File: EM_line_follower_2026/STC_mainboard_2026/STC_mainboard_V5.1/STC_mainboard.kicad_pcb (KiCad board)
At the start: 2 copper layers, 105 x 86.5 mm, 114 parts, among them J1 Conn_01x04, J10 Conn_01x04, J11 WirePad, J12 WirePad, J13 Conn_01x02, J14 WirePad, J15 WirePad, J16 WirePad, J2 WirePad, J20 WirePad, J21 WirePad, J23 WirePad, J24 WirePad, J3 WirePad, J4 Conn_01x04, J5 WirePad, J6 WirePad, J7 WirePad, J8 WirePad, J9 Conn_01x04, SW1 SW_Push, SW3 SW_Push, U1 STC16H40K128_CoreBoard, U10 TPS54360DDA, U3 LSM6DSRTR, U4 LM1117-3.3V, U5 OPA2197xD, U6 OPA2197xD, U7 OPA2197xD

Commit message: update V5.1
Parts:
- removed J1: Conn_01x04, Connector_JST:JST_XH_B4B-XH-A_1x04_P2.50mm_Vertical
- added RST: Conn_02x04_Odd_Even, Connector_PinSocket_2.54mm:PinSocket_2x04_P2.54mm_Vertical, F.Cu at (80.7, 209.9)
- added SW2: SW_Push, em1:SW-TH_L21.0-W15.0-KCD1-103, F.Cu at (59.0, 207.0)
- added SW4: SW_Push, em1:SW-TH_L21.0-W15.0-KCD1-103, F.Cu at (126.0, 133.0)
- C5, C6: moved to B.Cu
- moved J10 43.4 mm to (95.7, 209.6), turned to 180 degrees
- moved J4 7.19 mm to (118.9, 207.9)
- moved J9 7.19 mm to (128.8, 207.9)
- moved 1 6.88 mm to (135.8, 151.5)
- moved 111 6.88 mm to (126.9, 151.3)
- moved 11 6.88 mm to (131.5, 149.2)
- moved J13 6.88 mm to (132.5, 144.5)
- moved C2 4.84 mm to (142.5, 138.2)
- moved D22 4.84 mm to (142.5, 150.5)
- moved J20 4.84 mm to (137.5, 137.7)
- moved J21 4.84 mm to (140.0, 137.8)
- moved R60 4.84 mm to (142.3, 148.5)
- moved U9 4.84 mm to (139.4, 143.0)
- moved C12 3.80 mm to (86.4, 178.6)
- moved R10 3.80 mm to (87.2, 176.3)
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- renumbered RV3 to L1, RV2 to L2, RV4 to L3, RV1 to L4, RV5 to L5, L1 to L7
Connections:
- 111 pad 2: +12V -> /Vin
- J13 pad 2: +12V -> /Vin
- U1 pad 2: +5V -> Net-(U1-VCC)
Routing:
- net +5V: track 363.9 -> 301.1 mm
- net /P6.3: track 60.0 -> 8.11 mm
- net /P6.5: track 48.8 -> 11.2 mm
- net /P0.7: track 0.00 -> 32.4 mm
- net Net-(U1-VCC): track 0.00 -> 21.0 mm
- net /Vin: track 0.00 -> 17.6 mm
- net /P4.2: track 21.7 -> 39.0 mm
- net /P6.4: track 78.7 -> 93.5 mm
- net /P6.6: track 77.6 -> 92.3 mm
- net /P5.3: track 20.6 -> 7.45 mm
- net +12V: track 143.0 -> 154.2 mm, vias 0 -> 2
- net /P6.2: track 82.9 -> 92.3 mm
- net /P5.2: track 13.9 -> 7.40 mm
- net /P0.1: track 14.9 -> 9.01 mm
- net /P1.7: track 12.7 -> 17.8 mm
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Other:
- board size 105 x 86.5 mm -> 105 x 92.5 mm

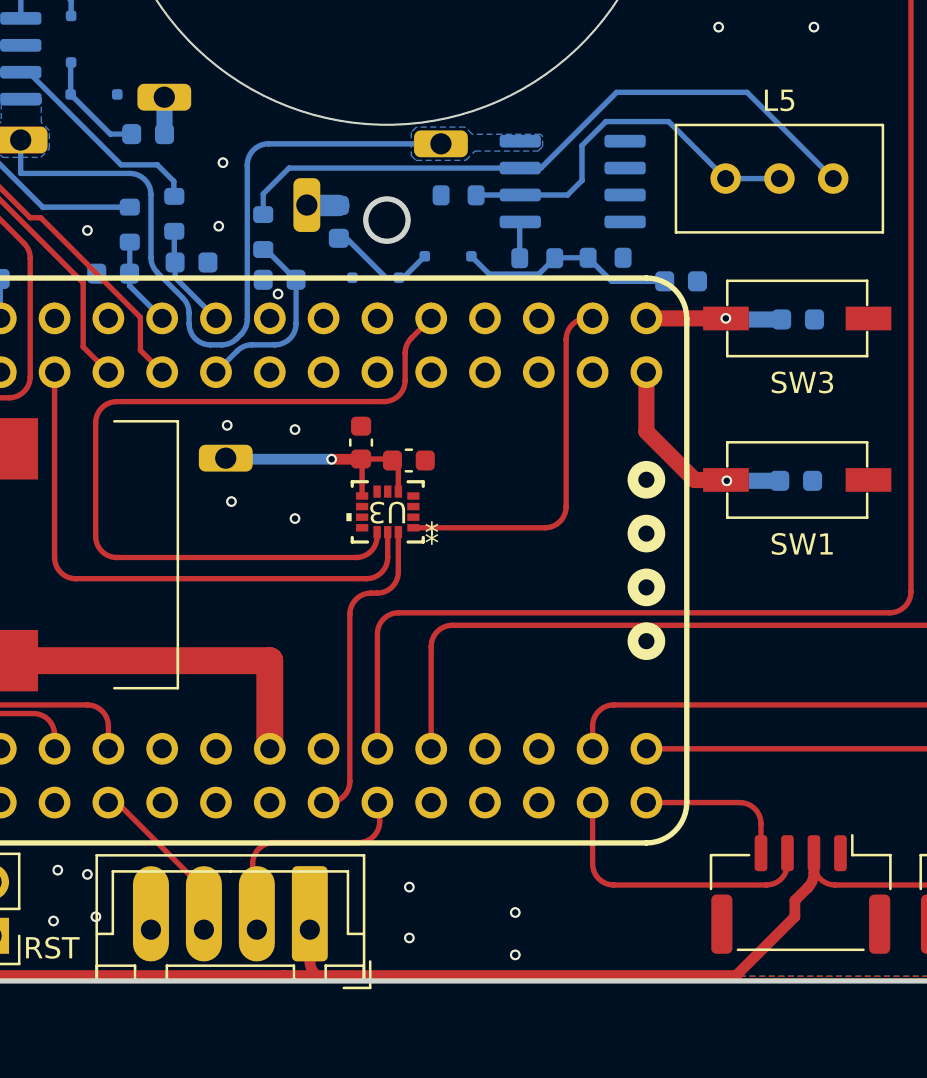
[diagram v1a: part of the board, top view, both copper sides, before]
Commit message: delete the extra hole for 5V
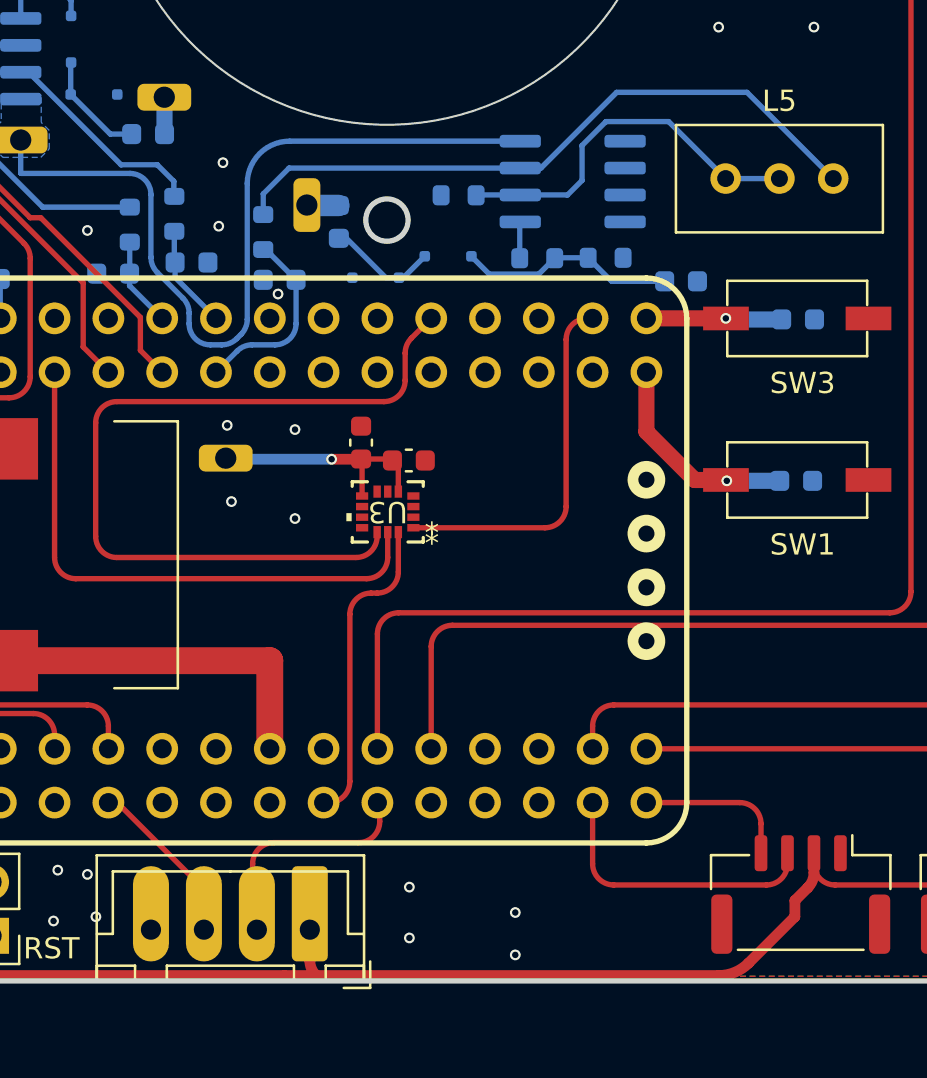
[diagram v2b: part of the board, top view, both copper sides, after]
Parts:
- removed J16: WirePad, STC_mainboard_lib:WirePad_motor
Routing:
- net +5V: track 301.1 -> 304.4 mm

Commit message: update wire(hole) position and step file as well
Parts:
- moved J2 29.1 mm to (124.6, 177.4)
- moved C33 26.0 mm to (123.0, 178.2)
- moved D19 21.7 mm to (120.5, 178.2), turned to 0 degrees
- moved R37 15.9 mm to (118.6, 175.0), turned to 90 degrees
- moved D24 14.8 mm to (117.0, 178.2), turned to 0 degrees
- moved R38 7.76 mm to (113.6, 175.0)
- moved L5 7.07 mm to (118.6, 167.3), turned to 90 degrees
- moved R36 3.92 mm to (113.6, 178.2), turned to 180 degrees
- moved C19 2.71 mm to (85.4, 172.4)
- moved C34 2.43 mm to (113.6, 176.6), turned to 180 degrees
- moved J8 2.05 mm to (88.8, 172.4)
- moved U6 0.17 mm to (108.3, 174.3)
- renumbered RST to J17
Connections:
- L5 pad 2: Net-(U6B--) -> Net-(U6A--)
- L5 pad 3: Net-(U6B--) -> Net-(U6A--)
- R37 pad 2: Net-(U6B--) -> Net-(U6A--)
- R38 pad 2: Net-(U6B-+) -> Net-(U6A-+)
- U6 pad 1: unconnected-(U6-Pad1) -> Net-(L5-Pad1)
- U6 pad 2: unconnected-(U6A---Pad2) -> Net-(U6A--)
- U6 pad 3: unconnected-(U6A-+-Pad3) -> Net-(U6A-+)
- U6 pad 5: Net-(U6B-+) -> unconnected-(U6B-+-Pad5)
- U6 pad 6: Net-(U6B--) -> unconnected-(U6B---Pad6)
- U6 pad 7: Net-(L5-Pad1) -> unconnected-(U6-Pad7)
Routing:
- net Net-(U6B--): track 17.8 -> 0.00 mm
- net Net-(U6A--): track 0.00 -> 14.7 mm
- net Net-(D24-K): track 10.3 -> 4.72 mm
- net Net-(U6A-+): track 0.00 -> 2.07 mm
- net Net-(L2-Pad1): track 34.3 -> 36.1 mm
- net Net-(U6B-+): track 1.73 -> 0.00 mm
- net Net-(D7-K): track 5.17 -> 3.82 mm
- net Net-(D19-K): track 5.08 -> 3.93 mm
- net Net-(L5-Pad1): track 31.6 -> 30.5 mm
- net /L2: track 1.74 -> 2.70 mm

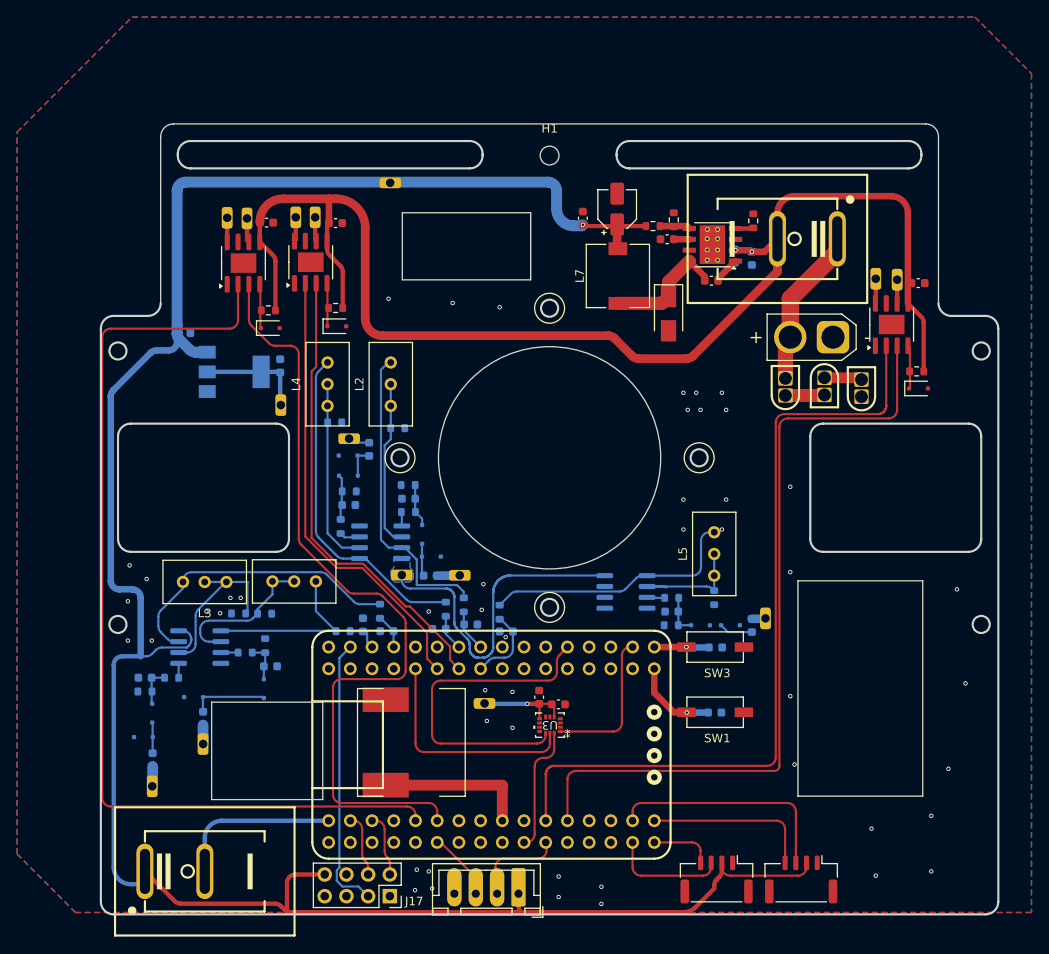
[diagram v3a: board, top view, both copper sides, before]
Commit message: update on board height
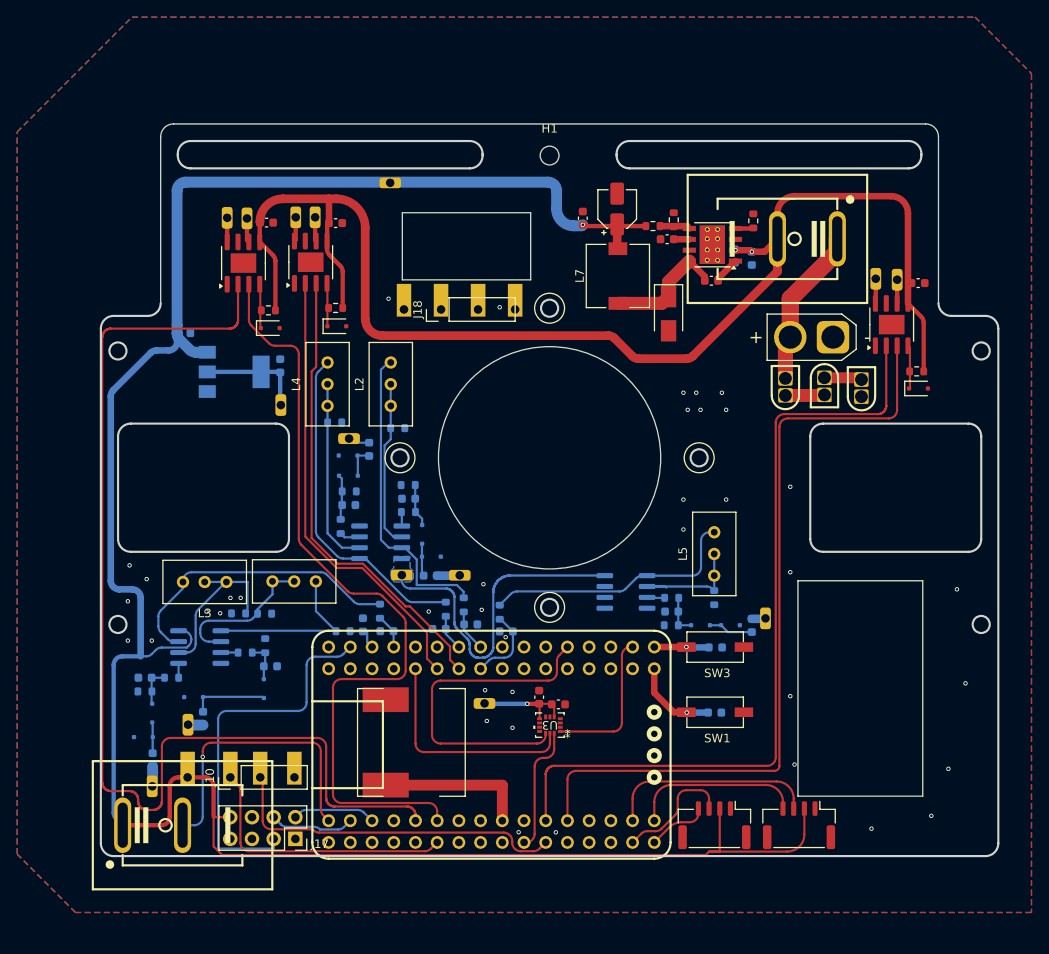
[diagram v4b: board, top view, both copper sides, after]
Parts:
- added J18: Conn_01x04, Connector_PinHeader_2.54mm:PinHeader_1x04_P2.54mm_Vertical, F.Cu at (86.3, 141.3)
- J10: footprint Connector_JST:JST_XH_B4B-XH-A_1x04_P2.50mm_Vertical -> Connector_PinHeader_2.54mm:PinHeader_1x04_P2.54mm_Vertical
- moved J10 36.4 mm to (62.0, 196.0), turned to 90 degrees
- moved J17 12.9 mm to (69.6, 203.2)
- moved J4 6.35 mm to (118.6, 201.6)
- moved J9 6.35 mm to (128.5, 201.6)
- moved SW2 5.99 mm to (56.4, 201.6)
- moved J5 2.86 mm to (57.0, 189.8)
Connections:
- J10 pad 2: /P6.5 -> /P6.3
- J10 pad 3: /P6.3 -> /P6.5
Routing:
- net /P6.5: track 11.2 -> 40.6 mm
- net /P6.3: track 8.11 -> 32.0 mm
- net /P6.0: track 113.4 -> 127.8 mm
- net Net-(U1-VCC): track 21.0 -> 33.9 mm, vias 0 -> 1
- net /P0.7: track 32.4 -> 44.6 mm
- net /P3.4: track 27.2 -> 24.7 mm
- net /P5.2: track 7.40 -> 9.85 mm
- net /P5.3: track 7.45 -> 9.75 mm
- net Net-(D19-K): track 3.93 -> 5.23 mm
- net +5V: track 304.1 -> 304.7 mm
- net GND: vias 49 -> 39
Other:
- board size 105 x 92.5 mm -> 105 x 85.7 mm
